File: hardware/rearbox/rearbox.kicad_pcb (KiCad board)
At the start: 4 copper layers, 80 x 60 mm, 222 parts, among them IC2 TPS54202HDDCR, J1 STDC14, J2 ST-LINK, J3 Conn_02x28_Top_Bottom, J4 Auxiliary, J5 XIAO ESP32S3 Sense, Q1 BUK6D210, Q2 BUK6D210, Q6 BUK6D210, U1 LM4040C33FTA, U10 TLP291-4, U11 TLP291-4, U12 TLP291-4, U17 MCP6N11T-002, U18 MCP6001, U19 MCP6N11T-002, U2 STM32G473RCTx, U20 MCP6001, U21 MCP6N11T-002, U22 MCP6001, U23 MCP6N11T-002, U24 MCP6001, U4 TLV743P, U7 ADM3057ExRW, U9 TCA6416ARTWR, Y1 48MHz

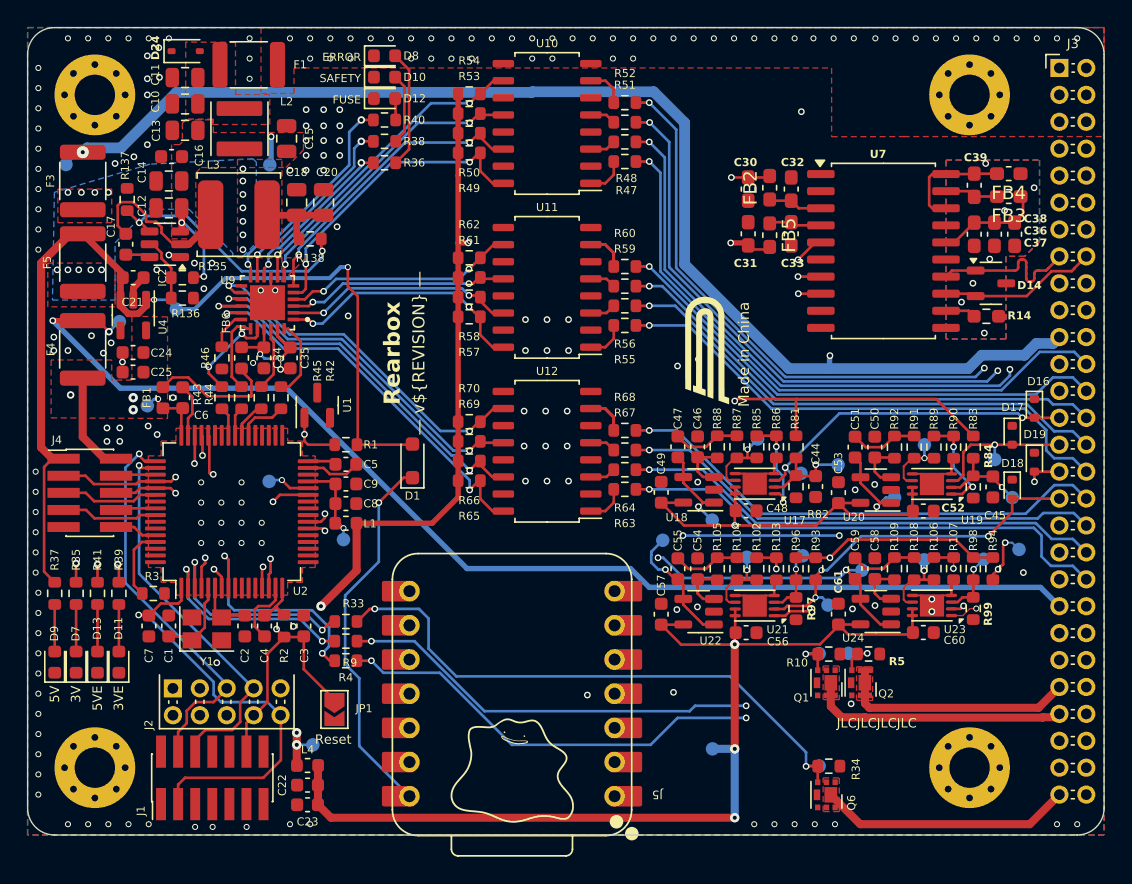
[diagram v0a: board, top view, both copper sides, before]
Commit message: Added an auxillary RTDS transistor as a backup
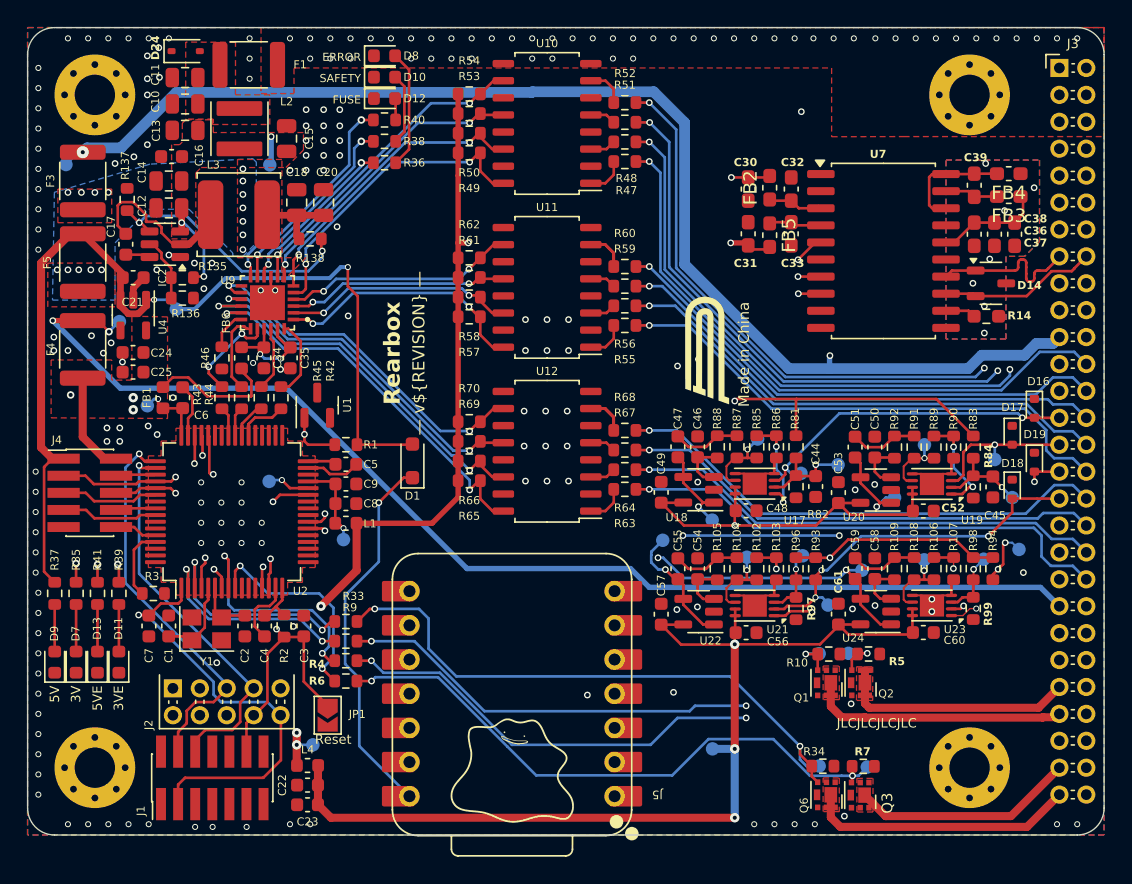
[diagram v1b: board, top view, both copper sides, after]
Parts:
- added Q3: BUK6D210, Local_Library:Diodes_UDFN2020-6_Type-F, F.Cu at (165.9, 131.0)
- added R6: 100R, Resistor_SMD:R_0603_1608Metric, F.Cu at (127.7, 122.6)
- added R7: 10k, Resistor_SMD:R_0603_1608Metric, F.Cu at (166.1, 128.9)
- added TP6: TestPoint_Small, TestPoint:TestPoint_Pad_D1.0mm, B.Cu at (166.4, 128.9)
- moved JP1 0.66 mm to (126.3, 125.1)
- moved R34 0.44 mm to (163.1, 128.9)
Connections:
- J3 pad 53: unconnected-(J3-Pin_53-Pad53) -> BACKUP_RTDS_OUT
- U2 pad 9: unconnected-(U2-PC1-Pad9) -> /BACKUP_RTDS
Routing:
- net Net-(Q3-G): track 0.00 -> 44.8 mm, vias 0 -> 2
- net BACKUP_RTDS_OUT: track 0.00 -> 16.6 mm
- net /BACKUP_RTDS: track 0.00 -> 16.2 mm, vias 0 -> 2
- net Net-(Q6-G): track 43.5 -> 44.7 mm
- net RTDS_OUT: track 18.8 -> 19.9 mm
- added copper zone on F.Cu, net BACKUP_RTDS_OUT

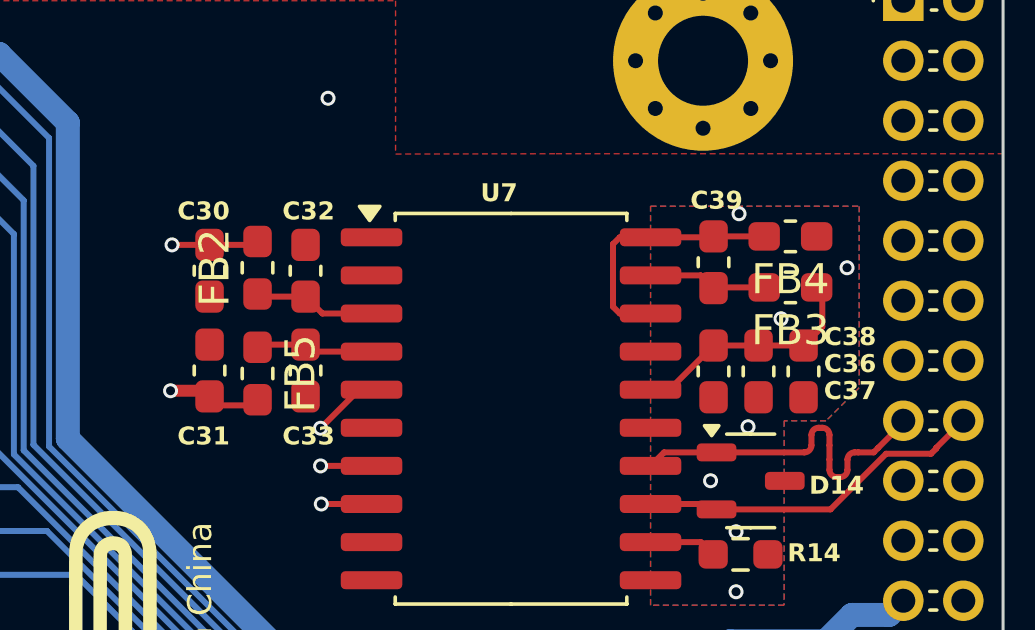
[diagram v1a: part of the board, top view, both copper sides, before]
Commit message: Made ferrites into 0805's
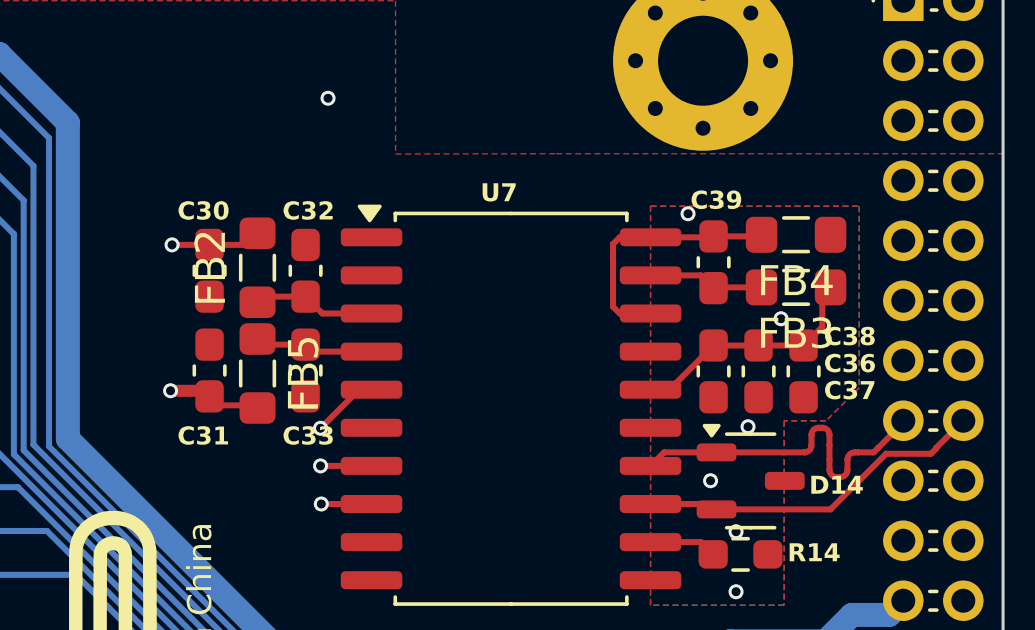
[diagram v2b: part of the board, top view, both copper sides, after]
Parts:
- FB2, FB3, FB4, FB5: footprint Inductor_SMD:L_0603_1608Metric_Pad1.05x0.95mm_HandSolder -> Inductor_SMD:L_0805_2012Metric_Pad1.05x1.20mm_HandSolder
- moved FB4 0.20 mm to (177.1, 84.8)
- moved FB3 0.19 mm to (177.1, 86.6)
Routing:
- net /CAN Transceivers/CAN Transceiver/GNDISO_CAN: vias 7 -> 6
